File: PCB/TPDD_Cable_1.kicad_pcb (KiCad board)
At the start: 2 copper layers, 10.4 x 13.2 mm, 11 parts, among them J2 TPDD, P2 RX, P20 DSR, P3 TX, P4 CTS, P5 RTS, P6 DTR, P7 GND, Q1 DTA114EKA, Q2 DTA114EKA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

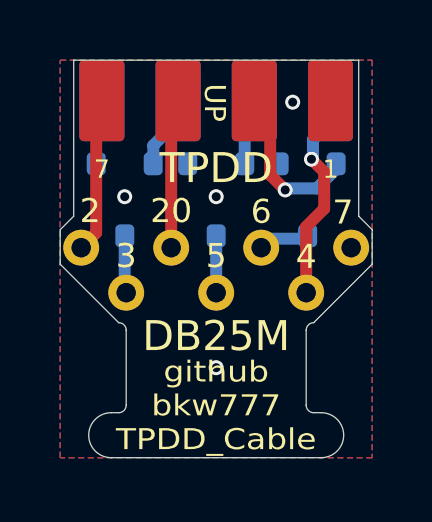
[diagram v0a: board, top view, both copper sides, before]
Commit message: pcb 2 is new default, smt wire pads
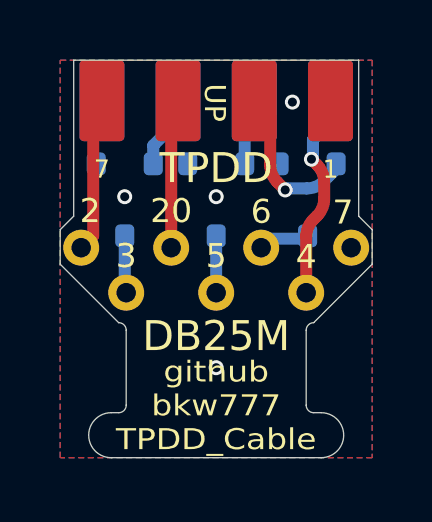
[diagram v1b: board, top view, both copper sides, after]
